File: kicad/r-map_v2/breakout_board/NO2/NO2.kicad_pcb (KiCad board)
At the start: 2 copper layers, 33 x 21.6 mm, 20 parts, among them P1 CONN_01X05, P2 CONN_01X05, Q1 2N7002, Q2 2N7002, U1 MICS-4514

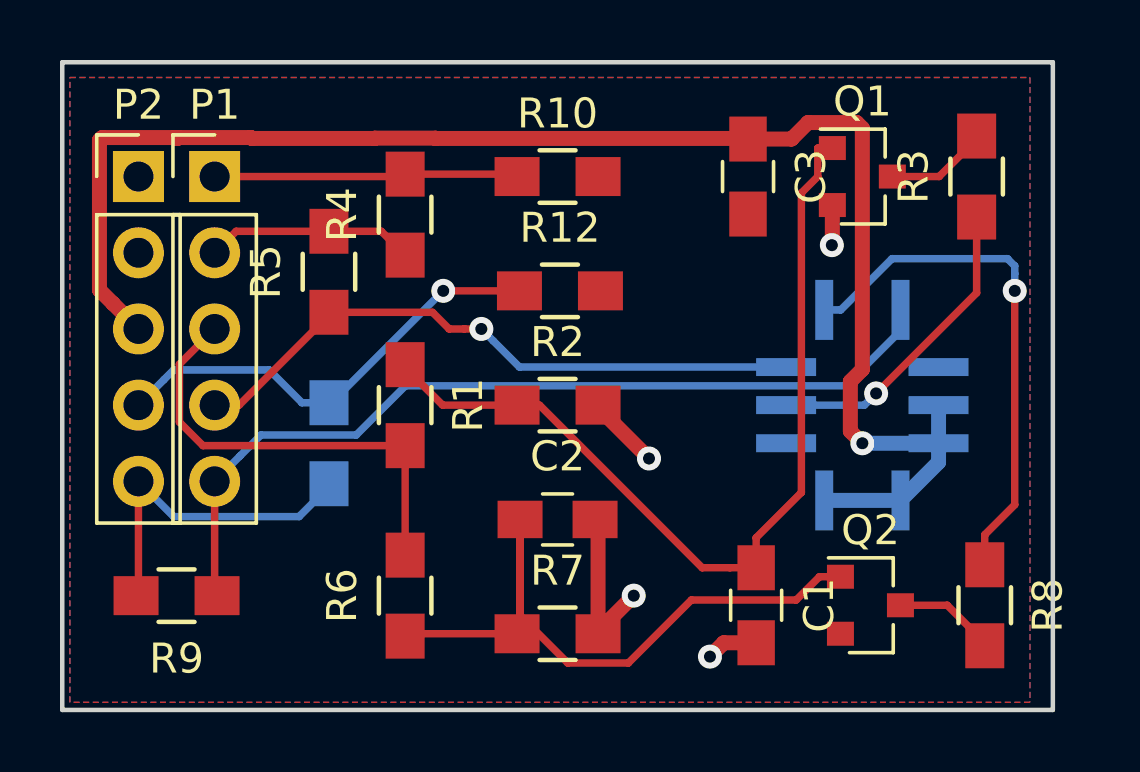
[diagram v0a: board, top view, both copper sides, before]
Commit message: Change of label and digital pin assignement on NO2 schematic
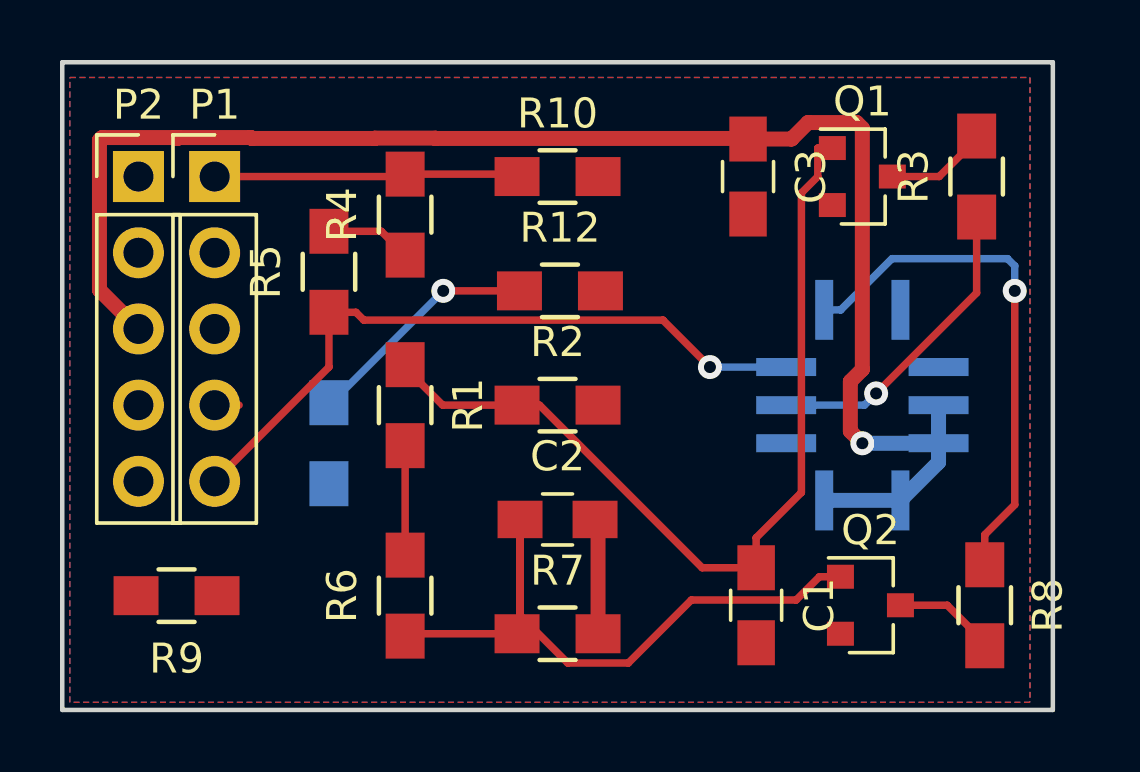
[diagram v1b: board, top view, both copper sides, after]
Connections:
- net D2 renamed NO2_SCALE_2
- P1 pad 2: D1 -> CO_SCALE_1
- P1 pad 3: D9 -> CO_SCALE_2
- P1 pad 4: A0 -> CO
- P1 pad 5: A1 -> NO2
- P2 pad 1: (no net) -> Net-(P2-Pad1)
- P2 pad 4: D4 -> FET
- P2 pad 5: D3 -> NO2_SCALE_1
- R1 pad 2: D9 -> FET
- R11 pad 1: D3 -> CO_SCALE_1
- R11 pad 2: D4 -> CO_SCALE_2
- R12 pad 1: D4 -> CO_SCALE_2
- R4 pad 1: D1 -> NO2_SCALE_1
- R5 pad 1: A0 -> NO2
- R5 pad 2: D1 -> NO2_SCALE_1
- R6 pad 2: D9 -> FET
- R9 pad 1: A1 -> CO
- R9 pad 2: D3 -> CO_SCALE_1
- U1 pad 1: (no net) -> Net-(U1-Pad1)
- U1 pad 3: A0 -> NO2
- U1 pad 5: A1 -> CO
- U1 pad 6: (no net) -> Net-(U1-Pad6)
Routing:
- net A1: track 29.5 -> 0.00 mm
- net NO2: track 0.00 -> 23.8 mm, vias 0 -> 1
- net A0: track 21.8 -> 0.00 mm, vias 1 -> 0
- net D4: track 15.2 -> 0.00 mm, vias 1 -> 0
- net D9: track 15.1 -> 0.00 mm
- net D3: track 11.2 -> 0.00 mm
- net CO_SCALE_2: track 0.00 -> 7.90 mm, vias 0 -> 1
- net GND: track 11.3 -> 4.11 mm, vias 4 -> 0
- net D1: track 6.98 -> 0.00 mm
- net FET: track 0.00 -> 3.65 mm
- net NO2_SCALE_1: track 0.00 -> 2.87 mm
- net CO: track 0.00 -> 1.63 mm
